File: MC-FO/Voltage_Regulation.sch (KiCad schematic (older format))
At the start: 8 parts, among them U19 R-78E5.0-0.5, U20 R-78E3.3-0.5

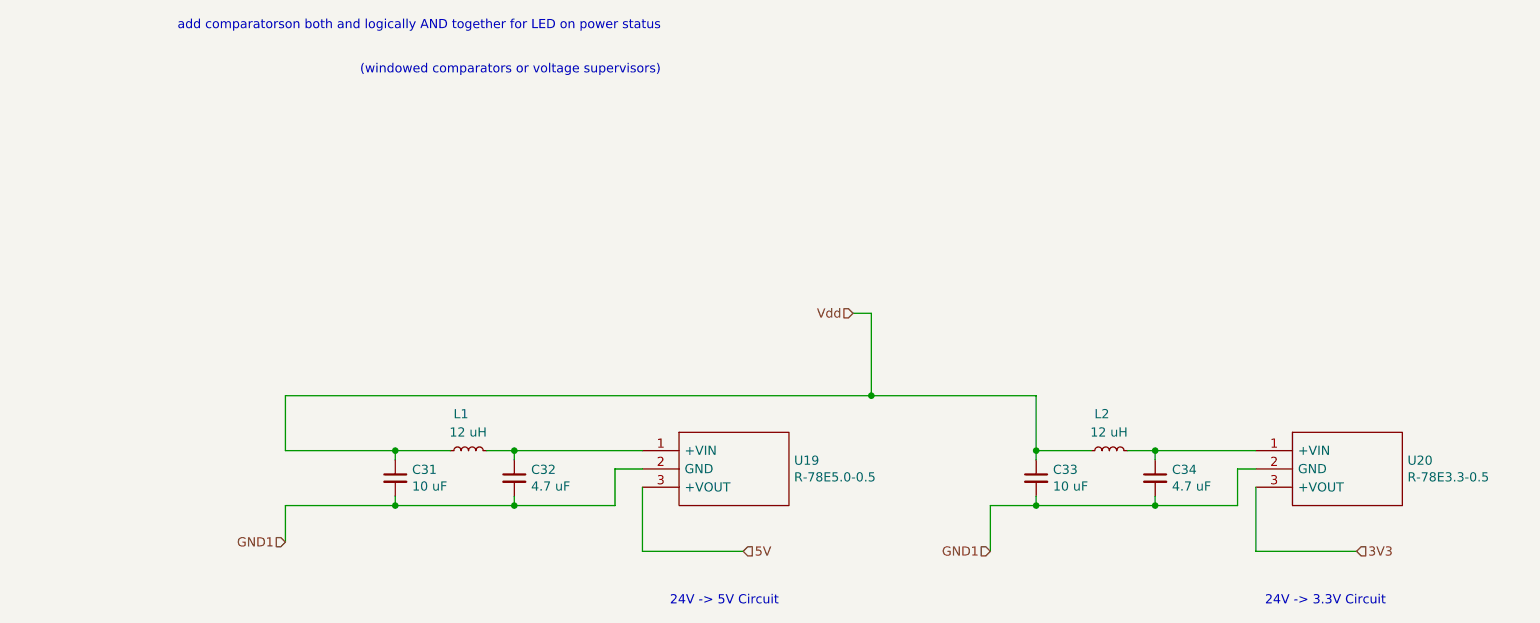
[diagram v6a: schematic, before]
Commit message: C31-34 larger packaging and part assignment
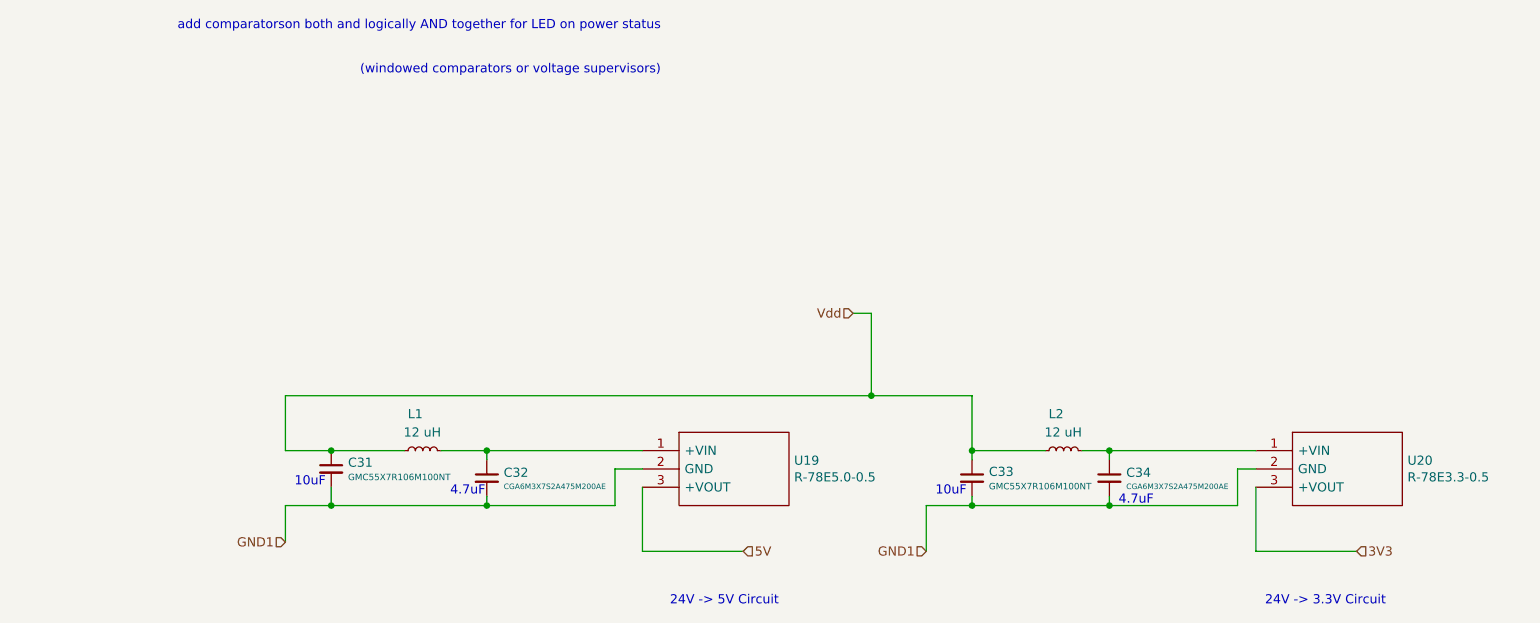
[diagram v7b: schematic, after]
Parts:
- removed C31, C33: 10 uF, Capacitor_SMD:C_0603_1608Metric, symbol Device:C_Small
- removed C32, C34: 4.7 uF, Capacitor_SMD:C_0603_1608Metric, symbol Device:C_Small
- added C31, C33: GMC55X7R106M100NT, Capacitor_SMD:C_2220_5650Metric, symbol Existing_IC_Models:GMC55X7R106M100NT
- added C32, C34: CGA6M3X7S2A475M200AE, Capacitor_SMD:C_1210_3225Metric, symbol Existing_IC_Models:CGA6M3X7S2A475M200AE
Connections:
- net GND1: now also C31.2, C32.2, C33.2, C34.2
- net Vdd: now also C31.1, C33.1
- net at L1.2, U19.1 (+VIN): now also C32.1
- net at L2.2, U20.1 (+VIN): now also C34.1
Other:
- note added: "10uF"
- note added: "4.7uF"
- moved on the sheet: L1, L2
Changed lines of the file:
@@
 Text HLabel 1650 5100 0    50   Input ~ 0
 GND1
-Text HLabel 5500 5150 0    50   Input ~ 0
+Text HLabel 5150 5150 0    50   Input ~ 0
 GND1
-$Comp
-L Device:C_Small C31
-U 1 1 61765AF4
-P 2250 4750
-F 0 "C31" H 2342 4796 50  0000 L CNN
-F 1 "10 uF" H 2342 4705 50  0000 L CNN
-F 2 "Capacitor_SMD:C_0603_1608Metric" H 2250 4750 50  0001 C CNN
-F 3 "~" H 2250 4750 50  0001 C CNN
-	1    2250 4750
-	1    0    0    -1
-$EndComp
-$Comp
-L Device:C_Small C32
-U 1 1 61766D82
-P 2900 4750
-F 0 "C32" H 2992 4796 50  0000 L CNN
-F 1 "4.7 uF" H 2992 4705 50  0000 L CNN
-F 2 "Capacitor_SMD:C_0603_1608Metric" H 2900 4750 50  0001 C CNN
-F 3 "~" H 2900 4750 50  0001 C CNN
-	1    2900 4750
-	1    0    0    -1
-$EndComp
 $Comp
 L Device:L_Small L1
 U 1 1 61767909
-P 2650 4600
-F 0 "L1" V 2850 4600 50  0000 L CNN
-F 1 "12 uH" V 2750 4500 50  0000 L CNN
-F 2 "Inductor_SMD:L_0603_1608Metric" H 2650 4600 50  0001 C CNN
-F 3 "~" H 2650 4600 50  0001 C CNN
-	1    2650 4600
+P 2400 4600
+F 0 "L1" V 2600 4600 50  0000 L CNN
+F 1 "12 uH" V 2500 4500 50  0000 L CNN
+F 2 "Inductor_SMD:L_0603_1608Metric" H 2400 4600 50  0001 C CNN
+F 3 "~" H 2400 4600 50  0001 C CNN
+	1    2400 4600
 	0    -1   -1   0
 $EndComp
@@
 	1650 4300 4850 4300
 Wire Wire Line
-	2550 4600 2250 4600
+	2500 4600 2750 4600
 Wire Wire Line
-	2250 4600 2250 4650
+	2750 4600 2750 4650
 Wire Wire Line
-	2250 4600 1650 4600
-Connection ~ 2250 4600
+	2750 4600 3600 4600
+Connection ~ 2750 4600
 Wire Wire Line
-	2750 4600 2900 4600
+	2750 4900 2750 4850
 Wire Wire Line
-	2900 4600 2900 4650
-Wire Wire Line
-	2900 4600 3600 4600
-Connection ~ 2900 4600
-Wire Wire Line
-	2250 4900 2250 4850
-Wire Wire Line
-	1650 4900 2250 4900
-Wire Wire Line
-	2250 4900 2900 4900
-Wire Wire Line
-	2900 4900 2900 4850
-Connection ~ 2250 4900
-Wire Wire Line
-	2900 4900 3450 4900
+	2750 4900 3450 4900
 Wire Wire Line
 	3450 4900 3450 4700
 Wire Wire Line
 	3450 4700 3600 4700
-Connection ~ 2900 4900
+Connection ~ 2750 4900
 Wire Wire Line
 	1650 4300 1650 4600
 $Comp
-L Device:C_Small C33
-U 1 1 61773A69
-P 5750 4750
-F 0 "C33" H 5842 4796 50  0000 L CNN
-F 1 "10 uF" H 5842 4705 50  0000 L CNN
-F 2 "Capacitor_SMD:C_0603_1608Metric" H 5750 4750 50  0001 C CNN
-F 3 "~" H 5750 4750 50  0001 C CNN
-	1    5750 4750
-	1    0    0    -1
-$EndComp
-$Comp
-L Device:C_Small C34
-U 1 1 61773ADF
-P 6400 4750
-F 0 "C34" H 6492 4796 50  0000 L CNN
-F 1 "4.7 uF" H 6492 4705 50  0000 L CNN
-F 2 "Capacitor_SMD:C_0603_1608Metric" H 6400 4750 50  0001 C CNN
-F 3 "~" H 6400 4750 50  0001 C CNN
-	1    6400 4750
-	1    0    0    -1
-$EndComp
-$Comp
 L Device:L_Small L2
 U 1 1 61773AE9
-P 6150 4600
-F 0 "L2" V 6350 4600 50  0000 L CNN
-F 1 "12 uH" V 6250 4500 50  0000 L CNN
-F 2 "Inductor_SMD:L_0603_1608Metric" H 6150 4600 50  0001 C CNN
-F 3 "~" H 6150 4600 50  0001 C CNN
-	1    6150 4600
+P 5900 4600
+F 0 "L2" V 6100 4600 50  0000 L CNN
+F 1 "12 uH" V 6000 4500 50  0000 L CNN
+F 2 "Inductor_SMD:L_0603_1608Metric" H 5900 4600 50  0001 C CNN
+F 3 "~" H 5900 4600 50  0001 C CNN
+	1    5900 4600
 	0    -1   -1   0
 $EndComp
 Wire Wire Line
-	6050 4600 5750 4600
+	5800 4600 5400 4600
 Wire Wire Line
-	5750 4600 5750 4650
+	5400 4600 5400 4650
 Wire Wire Line
-	6250 4600 6400 4600
+	6000 4600 6150 4600
 Wire Wire Line
-	6400 4600 6400 4650
+	6150 4600 6150 4650
 Wire Wire Line
-	5750 4900 5750 4850
+	5400 4900 5400 4850
 Wire Wire Line
-	5750 4900 6400 4900
+	5400 4900 6150 4900
 Wire Wire Line
-	6400 4900 6400 4850
+	6150 4900 6150 4850
 Wire Wire Line
-	5500 4900 5750 4900
+	5150 4900 5400 4900
 Wire Wire Line
-	5500 4900 5500 5150
-Connection ~ 5750 4900
+	5150 4900 5150 5150
+Connection ~ 5400 4900
 Wire Wire Line
-	5750 4300 5750 4600
+	4850 4300 5400 4300
 Wire Wire Line
-	4850 4300 5750 4300
-Connection ~ 5750 4600
+	6150 4600 6950 4600
+Connection ~ 6150 4600
 Wire Wire Line
-	6400 4600 6950 4600
-Connection ~ 6400 4600
-Wire Wire Line
-	6400 4900 6850 4900
+	6150 4900 6850 4900
 Wire Wire Line
 	6850 4900 6850 4700
 Wire Wire Line
 	6850 4700 6950 4700
-Connection ~ 6400 4900
+Connection ~ 6150 4900
 $Comp
 L Existing_IC_Models:R-78E3.3-0.5 U20
@@
 	1    0    0    -1
 $EndComp
+$Comp
+L Existing_IC_Models:GMC55X7R106M100NT C31
+U 1 1 617C2E30
+P 1900 4700
+F 0 "C31" H 1992 4735 50  0000 L CNN
+F 1 "GMC55X7R106M100NT" H 1992 4655 35  0000 L CNN
+F 2 "Capacitor_SMD:C_2220_5650Metric" H 1900 4700 50  0001 C CNN
+F 3 "https://www.digikey.com/en/products/detail/cal-chip-electronics-inc/GMC55X7R106M100NT/14288754" H 1900 4700 50  0001 C CNN
+	1    1900 4700
+	1    0    0    -1
+$EndComp
+Connection ~ 1900 4900
+Wire Wire Line
+	1900 4900 2750 4900
+Wire Wire Line
+	1650 4900 1900 4900
+Wire Wire Line
+	1900 4900 1900 4800
+Connection ~ 1900 4600
+Wire Wire Line
+	1900 4600 1650 4600
+Wire Wire Line
+	2300 4600 1900 4600
+$Comp
+L Existing_IC_Models:GMC55X7R106M100NT C33
+U 1 1 617C96A7
+P 5400 4750
+F 0 "C33" H 5492 4785 50  0000 L CNN
+F 1 "GMC55X7R106M100NT" H 5492 4705 35  0000 L CNN
+F 2 "Capacitor_SMD:C_2220_5650Metric" H 5400 4750 50  0001 C CNN
+F 3 "https://www.digikey.com/en/products/detail/cal-chip-electronics-inc/GMC55X7R106M100NT/14288754" H 5400 4750 50  0001 C CNN
+	1    5400 4750
+	1    0    0    -1
+$EndComp
+Wire Wire Line
+	5400 4300 5400 4600
+Connection ~ 5400 4600
+$Comp
+L Existing_IC_Models:CGA6M3X7S2A475M200AE C34
+U 1 1 617CD2CA
+P 6150 4750
+F 0 "C34" H 6242 4780 50  0000 L CNN
+F 1 "CGA6M3X7S2A475M200AE" H 6242 4704 30  0000 L CNN
+F 2 "Capacitor_SMD:C_1210_3225Metric" H 6150 4750 50  0001 C CNN
+F 3 "https://www.digikey.com/en/products/detail/tdk-corporation/CGA6M3X7S2A475M200AE/2782508" H 6150 4750 50  0001 C CNN
+	1    6150 4750
+	1    0    0    -1
+$EndComp
+$Comp
+L Existing_IC_Models:CGA6M3X7S2A475M200AE C32
+U 1 1 617D1DBC
+P 2750 4750
+F 0 "C32" H 2842 4780 50  0000 L CNN
+F 1 "CGA6M3X7S2A475M200AE" H 2842 4704 30  0000 L CNN
+F 2 "Capacitor_SMD:C_1210_3225Metric" H 2750 4750 50  0001 C CNN
+F 3 "https://www.digikey.com/en/products/detail/tdk-corporation/CGA6M3X7S2A475M200AE/2782508" H 2750 4750 50  0001 C CNN
+	1    2750 4750
+	1    0    0    -1
+$EndComp
+Text Notes 1700 4800 0    50   ~ 0
+10uF
+Text Notes 5200 4850 0    50   ~ 0
+10uF
+Text Notes 2550 4850 0    50   ~ 0
+4.7uF
+Text Notes 6200 4900 0    50   ~ 0
+4.7uF
 $EndSCHEMATC

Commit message: remove part # on Cap...getting ahead of myself
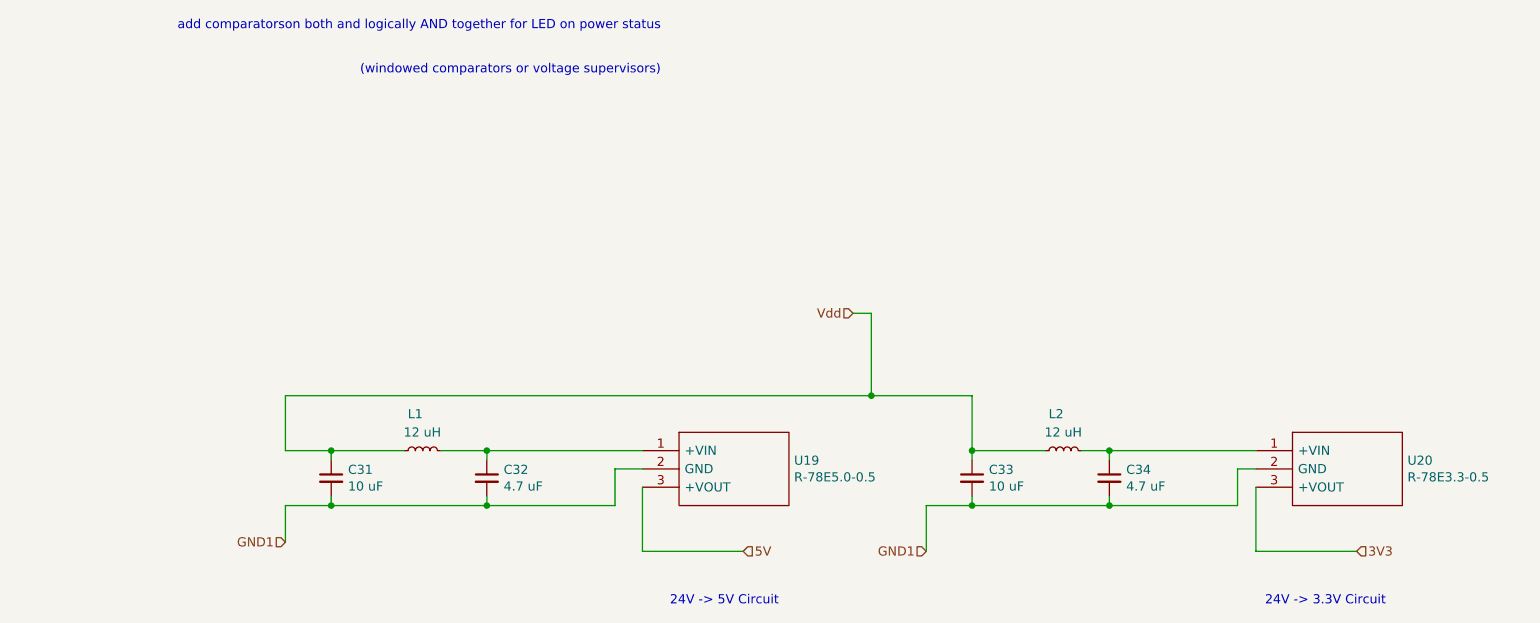
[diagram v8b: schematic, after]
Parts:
- removed C31, C33: GMC55X7R106M100NT, Capacitor_SMD:C_2220_5650Metric, symbol Existing_IC_Models:GMC55X7R106M100NT
- removed C32, C34: CGA6M3X7S2A475M200AE, Capacitor_SMD:C_1210_3225Metric, symbol Existing_IC_Models:CGA6M3X7S2A475M200AE
- added C31, C33: 10 uF, Capacitor_SMD:C_1210_3225Metric, symbol Device:C_Small
- added C32, C34: 4.7 uF, Capacitor_SMD:C_1210_3225Metric, symbol Device:C_Small
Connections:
- net GND1: now also C31.2, C32.2, C33.2, C34.2
- net Vdd: now also C31.1, C33.1
- net at L1.2, U19.1 (+VIN): now also C32.1
- net at L2.2, U20.1 (+VIN): now also C34.1
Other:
- note removed: "10uF"
- note removed: "4.7uF"
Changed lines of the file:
@@
-	1    0    0    -1
-$EndComp
-$Comp
-L Existing_IC_Models:GMC55X7R106M100NT C31
-U 1 1 617C2E30
-P 1900 4700
-F 0 "C31" H 1992 4735 50  0000 L CNN
-F 1 "GMC55X7R106M100NT" H 1992 4655 35  0000 L CNN
-F 2 "Capacitor_SMD:C_2220_5650Metric" H 1900 4700 50  0001 C CNN
-F 3 "https://www.digikey.com/en/products/detail/cal-chip-electronics-inc/GMC55X7R106M100NT/14288754" H 1900 4700 50  0001 C CNN
-	1    1900 4700
 	1    0    0    -1
 $EndComp
@@
 	1650 4900 1900 4900
 Wire Wire Line
-	1900 4900 1900 4800
-Connection ~ 1900 4600
-Wire Wire Line
-	1900 4600 1650 4600
-Wire Wire Line
-	2300 4600 1900 4600
-$Comp
-L Existing_IC_Models:GMC55X7R106M100NT C33
-U 1 1 617C96A7
-P 5400 4750
-F 0 "C33" H 5492 4785 50  0000 L CNN
-F 1 "GMC55X7R106M100NT" H 5492 4705 35  0000 L CNN
-F 2 "Capacitor_SMD:C_2220_5650Metric" H 5400 4750 50  0001 C CNN
-F 3 "https://www.digikey.com/en/products/detail/cal-chip-electronics-inc/GMC55X7R106M100NT/14288754" H 5400 4750 50  0001 C CNN
-	1    5400 4750
-	1    0    0    -1
-$EndComp
+	1900 4900 1900 4850
 Wire Wire Line
 	5400 4300 5400 4600
 Connection ~ 5400 4600
 $Comp
-L Existing_IC_Models:CGA6M3X7S2A475M200AE C34
-U 1 1 617CD2CA
+L Device:C_Small C31
+U 1 1 617DD2CC
+P 1900 4750
+F 0 "C31" H 1992 4796 50  0000 L CNN
+F 1 "10 uF" H 1992 4705 50  0000 L CNN
+F 2 "Capacitor_SMD:C_1210_3225Metric" H 1900 4750 50  0001 C CNN
+F 3 "~" H 1900 4750 50  0001 C CNN
+	1    1900 4750
+	1    0    0    -1
+$EndComp
+Wire Wire Line
+	2300 4600 1900 4600
+Wire Wire Line
+	1900 4650 1900 4600
+Connection ~ 1900 4600
+Wire Wire Line
+	1900 4600 1650 4600
+$Comp
+L Device:C_Small C32
+U 1 1 617DF962
+P 2750 4750
+F 0 "C32" H 2842 4796 50  0000 L CNN
+F 1 "4.7 uF" H 2842 4705 50  0000 L CNN
+F 2 "Capacitor_SMD:C_1210_3225Metric" H 2750 4750 50  0001 C CNN
+F 3 "~" H 2750 4750 50  0001 C CNN
+	1    2750 4750
+	1    0    0    -1
+$EndComp
+$Comp
+L Device:C_Small C34
+U 1 1 617E1CA5
 P 6150 4750
-F 0 "C34" H 6242 4780 50  0000 L CNN
-F 1 "CGA6M3X7S2A475M200AE" H 6242 4704 30  0000 L CNN
+F 0 "C34" H 6242 4796 50  0000 L CNN
+F 1 "4.7 uF" H 6242 4705 50  0000 L CNN
 F 2 "Capacitor_SMD:C_1210_3225Metric" H 6150 4750 50  0001 C CNN
-F 3 "https://www.digikey.com/en/products/detail/tdk-corporation/CGA6M3X7S2A475M200AE/2782508" H 6150 4750 50  0001 C CNN
+F 3 "~" H 6150 4750 50  0001 C CNN
 	1    6150 4750
 	1    0    0    -1
 $EndComp
 $Comp
-L Existing_IC_Models:CGA6M3X7S2A475M200AE C32
-U 1 1 617D1DBC
-P 2750 4750
-F 0 "C32" H 2842 4780 50  0000 L CNN
-F 1 "CGA6M3X7S2A475M200AE" H 2842 4704 30  0000 L CNN
-F 2 "Capacitor_SMD:C_1210_3225Metric" H 2750 4750 50  0001 C CNN
-F 3 "https://www.digikey.com/en/products/detail/tdk-corporation/CGA6M3X7S2A475M200AE/2782508" H 2750 4750 50  0001 C CNN
-	1    2750 4750
+L Device:C_Small C33
+U 1 1 617E2200
+P 5400 4750
+F 0 "C33" H 5492 4796 50  0000 L CNN
+F 1 "10 uF" H 5492 4705 50  0000 L CNN
+F 2 "Capacitor_SMD:C_1210_3225Metric" H 5400 4750 50  0001 C CNN
+F 3 "~" H 5400 4750 50  0001 C CNN
+	1    5400 4750
 	1    0    0    -1
 $EndComp
-Text Notes 1700 4800 0    50   ~ 0
-10uF
-Text Notes 5200 4850 0    50   ~ 0
-10uF
-Text Notes 2550 4850 0    50   ~ 0
-4.7uF
-Text Notes 6200 4900 0    50   ~ 0
-4.7uF
 $EndSCHEMATC
